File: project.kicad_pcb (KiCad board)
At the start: 4 copper layers, 0 parts

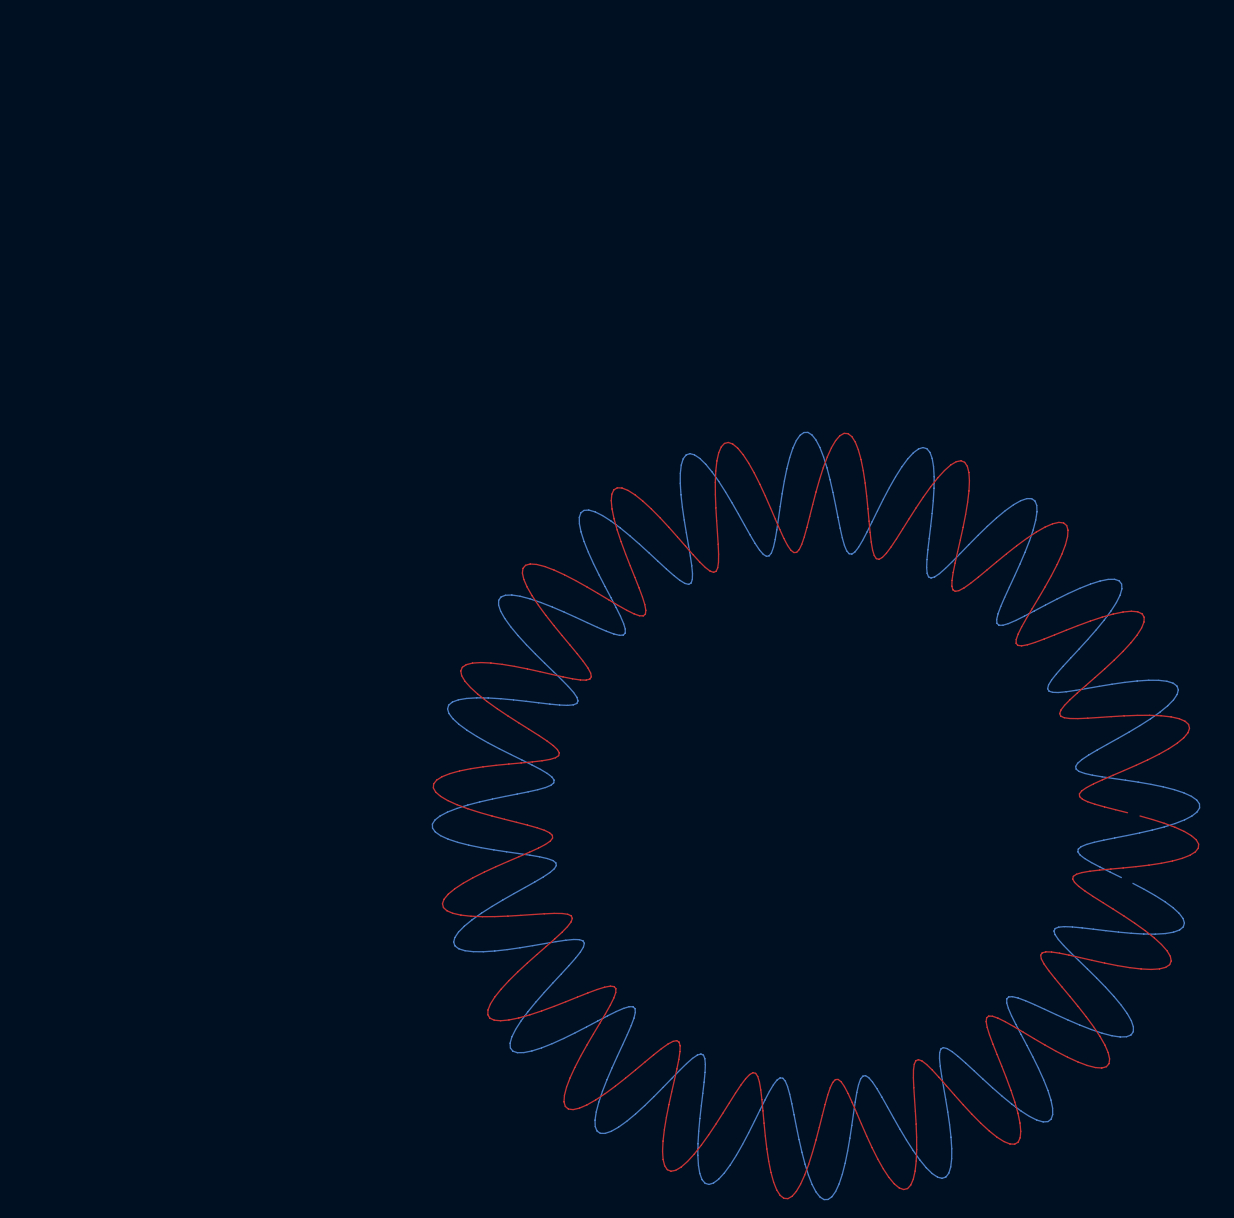
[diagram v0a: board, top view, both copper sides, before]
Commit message: Spiral pattern matches reference design now.
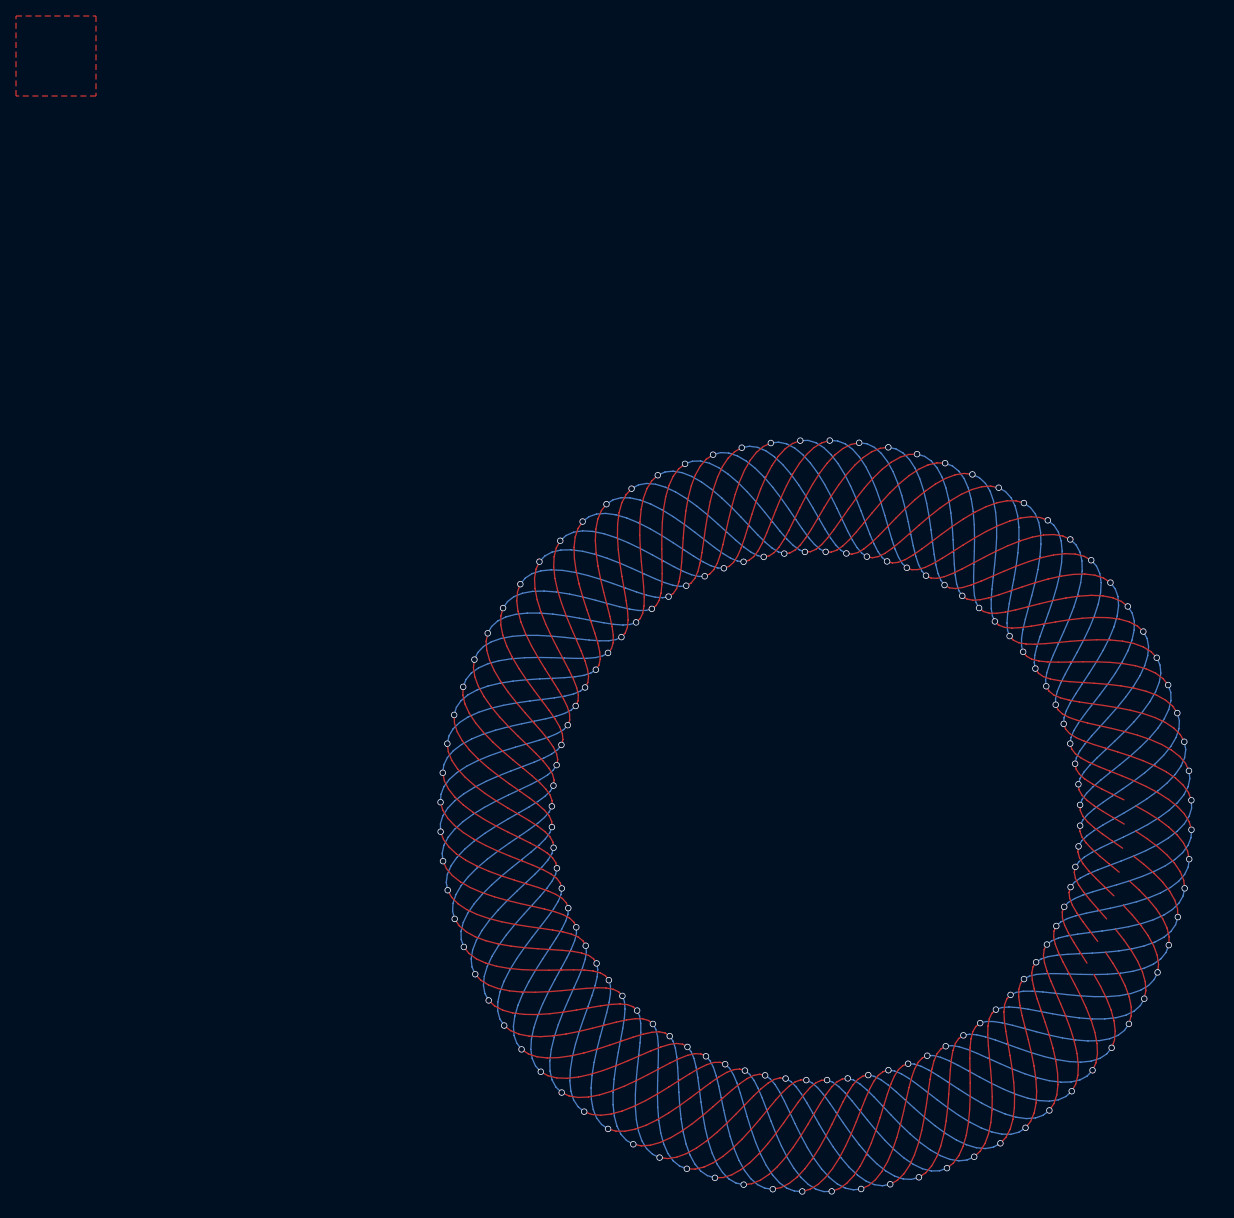
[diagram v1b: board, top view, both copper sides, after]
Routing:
- net RX2: track 667.5 -> 1164.4 mm, vias 0 -> 60
- net RX1: track 667.5 -> 1164.4 mm, vias 0 -> 60
- net TX: track 667.5 -> 776.3 mm, vias 0 -> 40
- added copper zone on B.Cu, net GND
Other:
- copper layers 4 -> 2

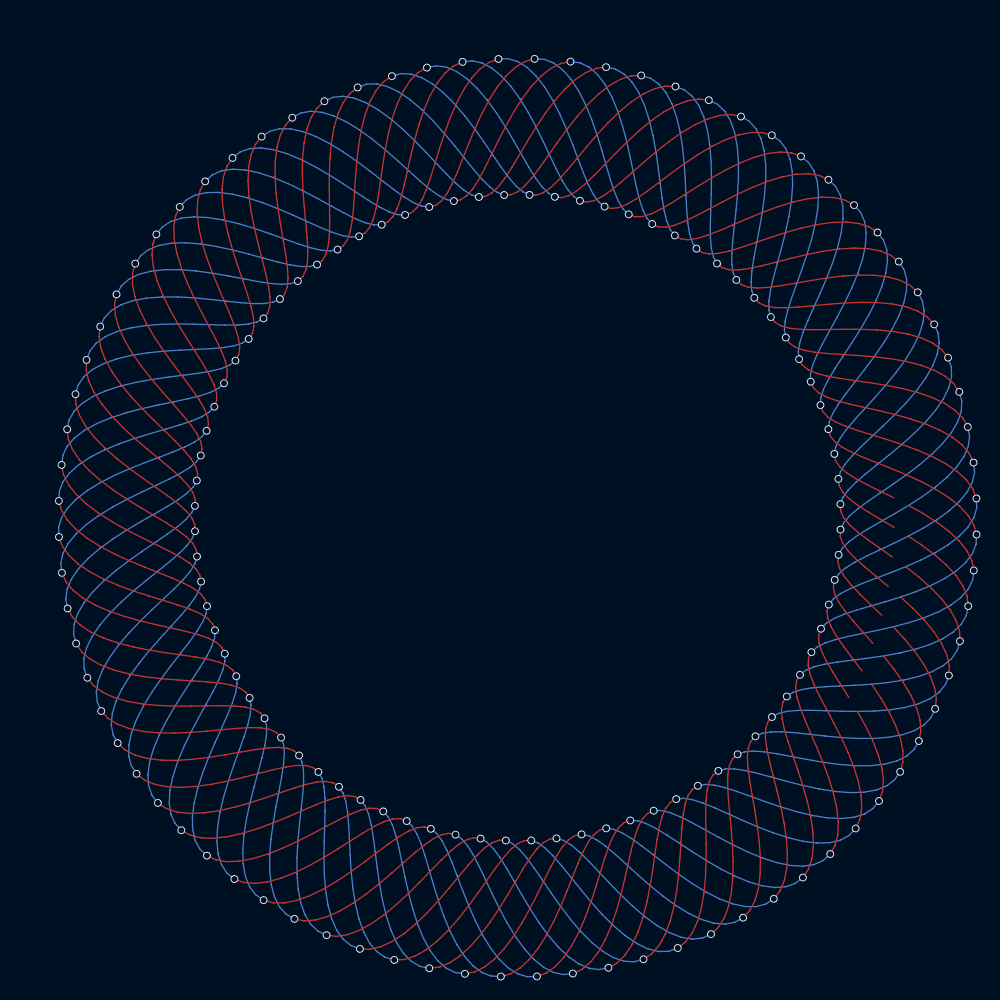
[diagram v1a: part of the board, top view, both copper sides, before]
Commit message: Complete loops that double back on one side using vias. Nets may be incorrect.
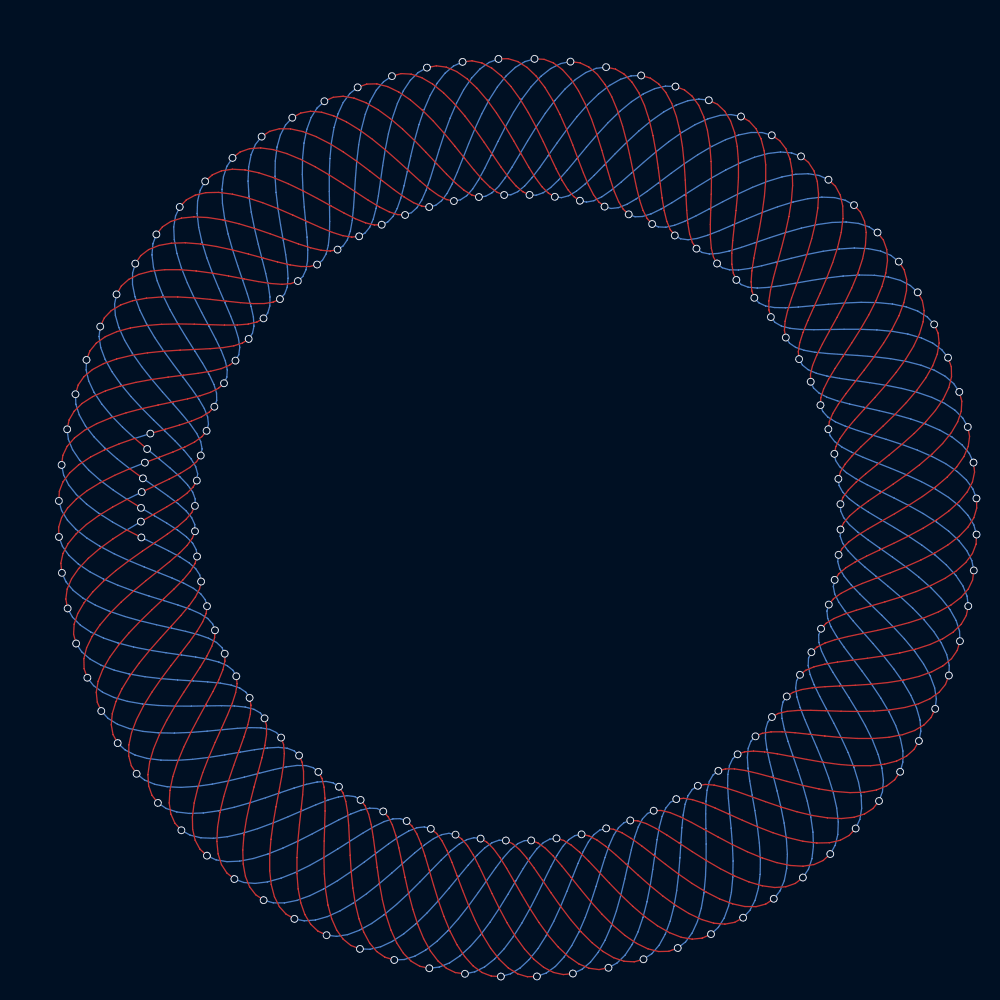
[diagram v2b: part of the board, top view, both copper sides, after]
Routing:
- net TX: track 776.3 -> 0.00 mm, vias 40 -> 0
- net RX2: track 1164.4 -> 1559.2 mm, vias 60 -> 84
- net RX1: track 1164.4 -> 1559.2 mm, vias 60 -> 84

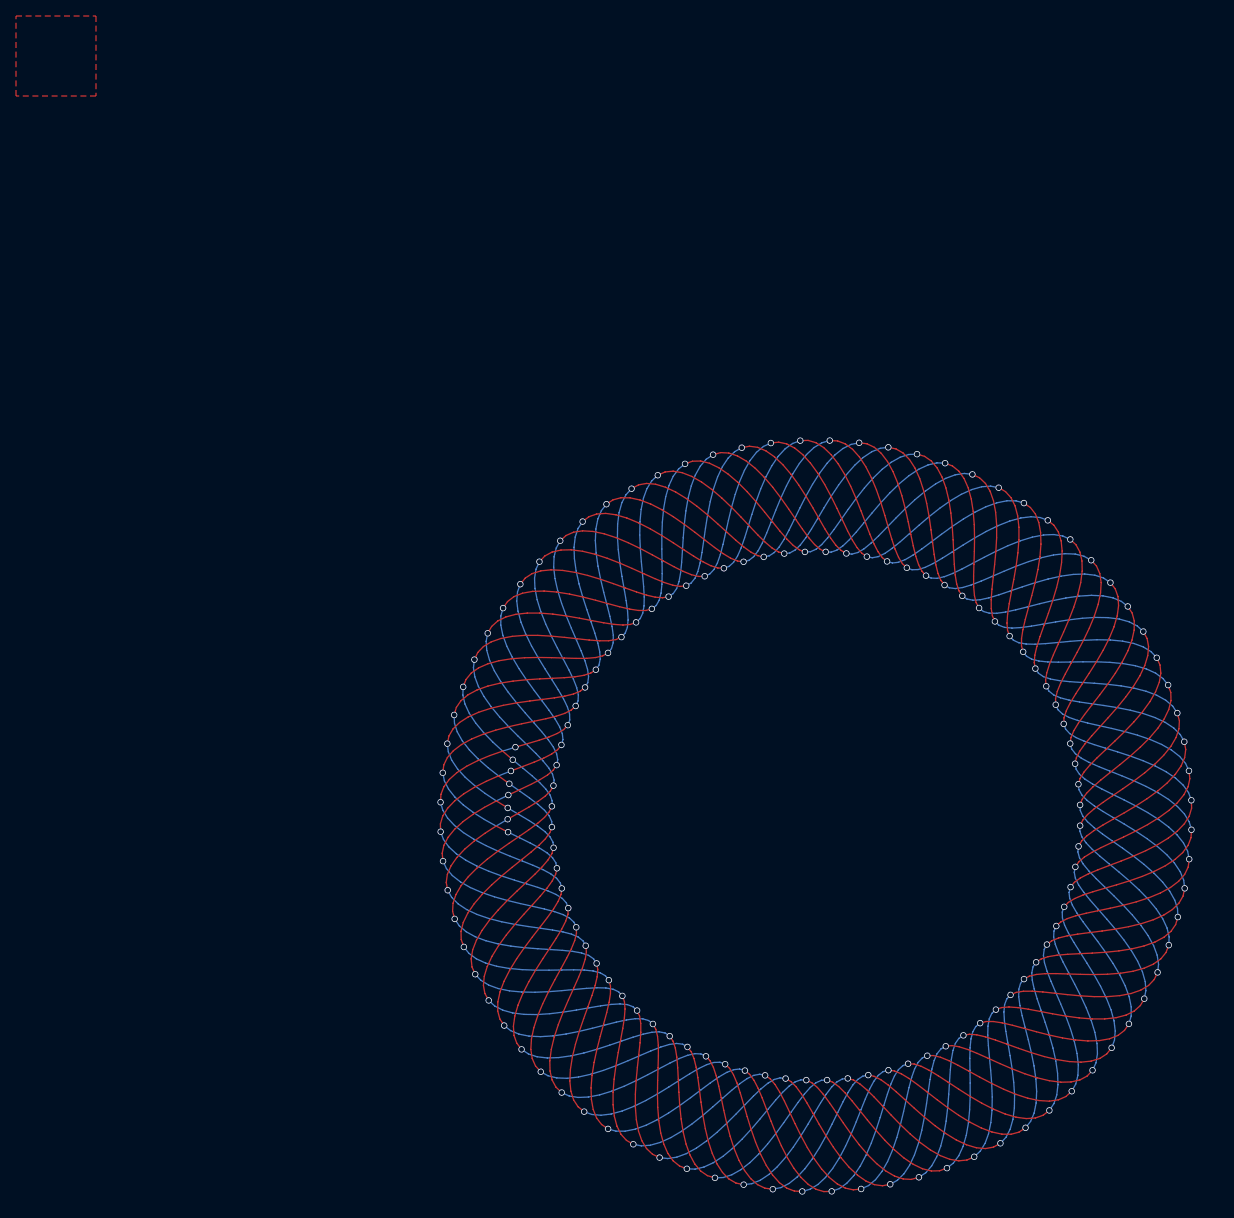
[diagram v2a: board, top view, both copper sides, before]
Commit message: Latest version now properly breaks out the coils and does the cross over patch. net labels still confused but copper looks good.
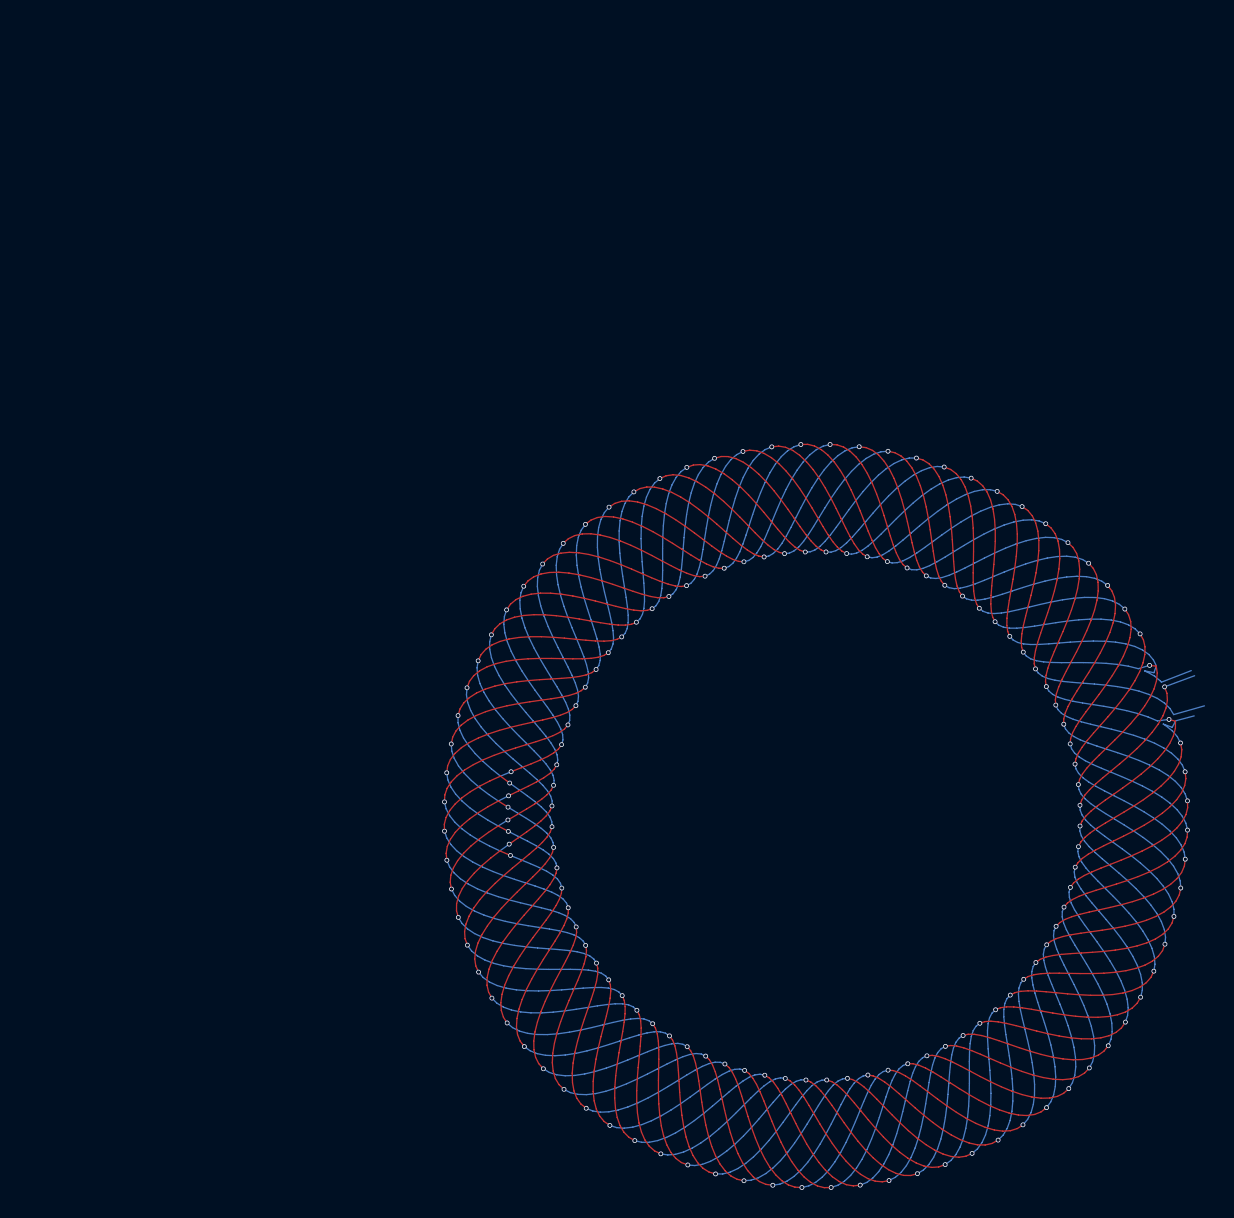
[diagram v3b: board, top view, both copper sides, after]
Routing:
- net RX2: track 1559.2 -> 0.00 mm, vias 84 -> 0
- net RX1: track 1559.2 -> 0.00 mm, vias 84 -> 0
- net 4: track 0.00 -> 391.9 mm, vias 0 -> 21
- net 6: track 0.00 -> 386.2 mm, vias 0 -> 21
- net 5: track 0.00 -> 385.0 mm, vias 0 -> 21
- net 8: track 0.00 -> 381.0 mm, vias 0 -> 21
- net 1: track 0.00 -> 381.0 mm, vias 0 -> 21
- net 7: track 0.00 -> 381.0 mm, vias 0 -> 21
- net 2: track 0.00 -> 381.0 mm, vias 0 -> 21
- net 3: track 0.00 -> 381.0 mm, vias 0 -> 21
- removed copper zone on B.Cu, net GND

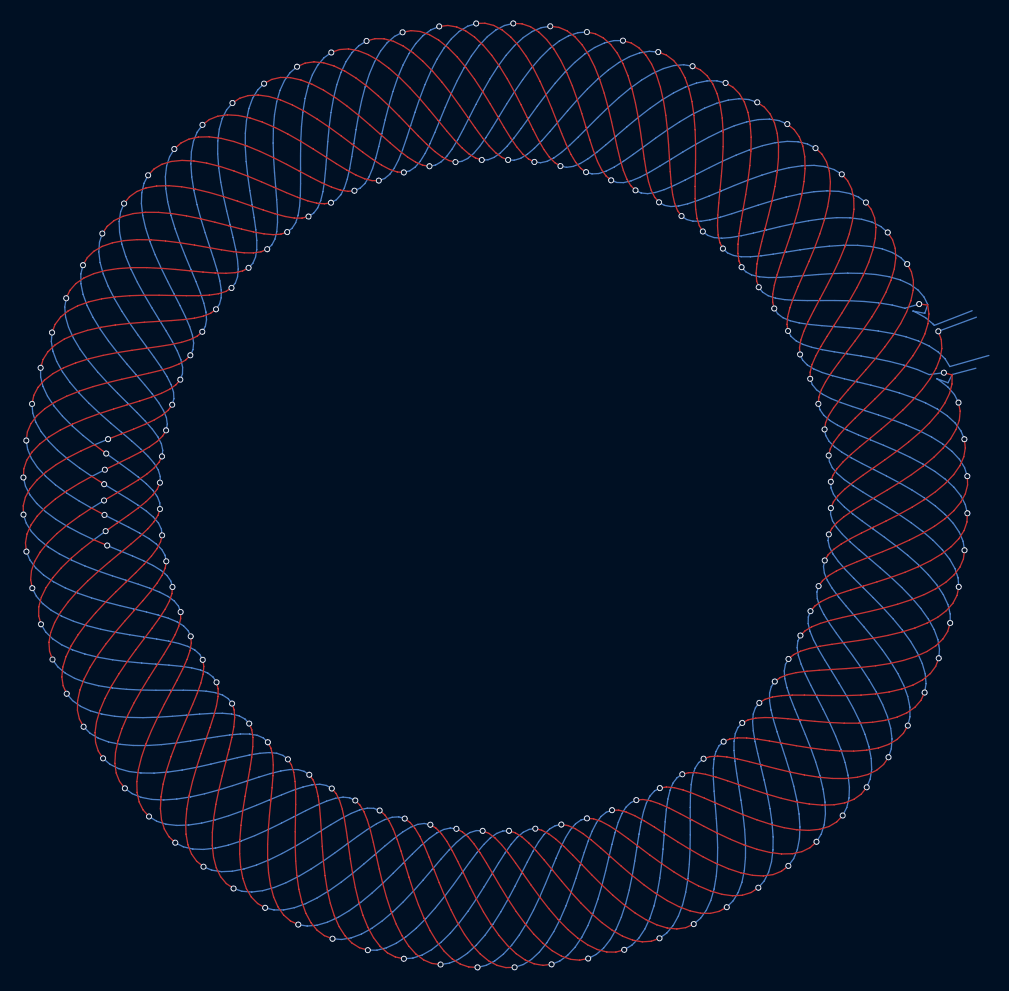
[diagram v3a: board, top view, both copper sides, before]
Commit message: Replaced sin function with equal area calculation. Many thanks to gitub user madcowswe aka Oskar Weigl from Odrive Robotics for the updated calculation!
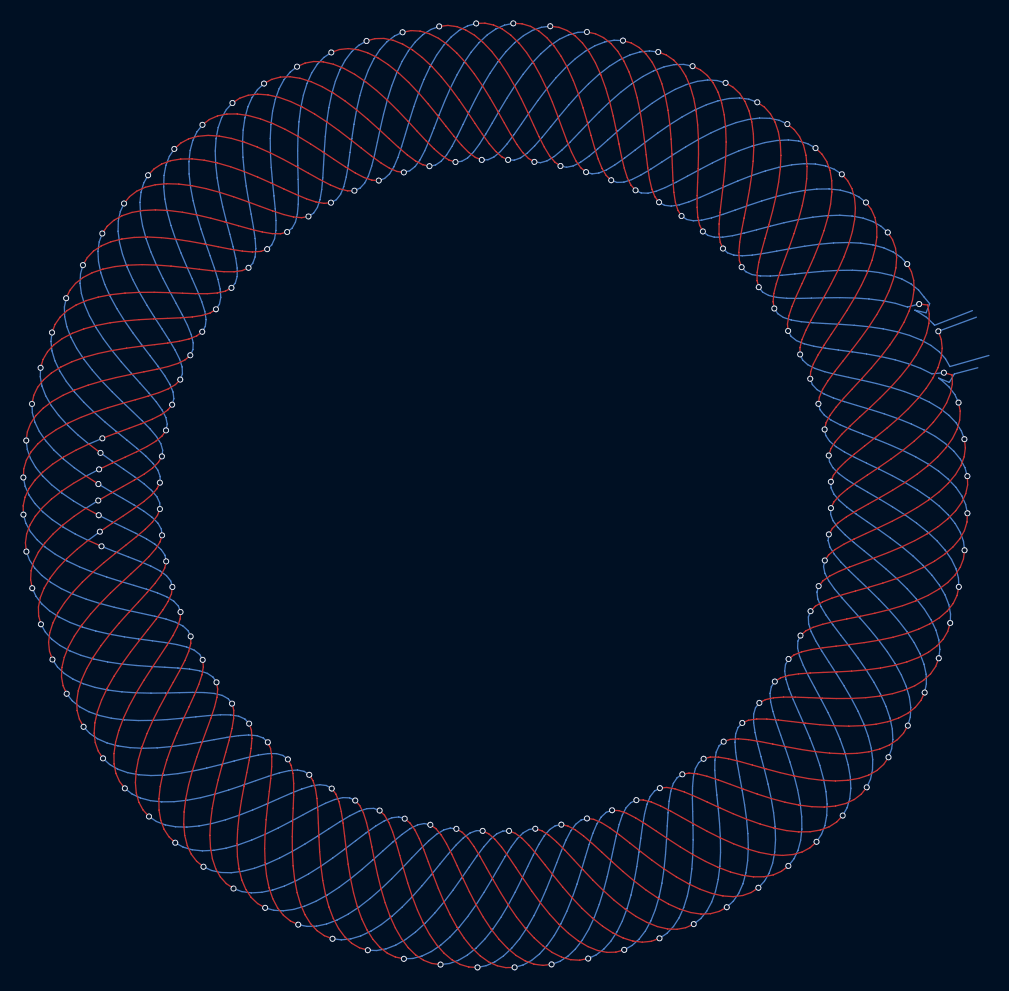
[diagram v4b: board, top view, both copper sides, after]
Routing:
- net 3: track 381.0 -> 382.9 mm
- net 5: track 385.0 -> 386.9 mm
- net 2: track 381.0 -> 382.9 mm
- net 7: track 381.0 -> 382.9 mm
- net 8: track 381.0 -> 382.9 mm
- net 1: track 381.0 -> 382.9 mm
- net 4: track 391.9 -> 393.6 mm
- net 6: track 386.2 -> 387.8 mm
